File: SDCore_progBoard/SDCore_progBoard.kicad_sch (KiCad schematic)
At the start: 7 parts, among them U1 BL1117-33CX

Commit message: Updated BOOTSEL logic
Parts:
- added SW1: TS-1101-C-W, JLCImport:TS-1101-C-W, symbol JLCImport:TS-1101-C-W
- renumbered USB2 to USB1
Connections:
- net +3V3: now also SW1.1; no longer Card1.6 (VSS2)
- new net: Card1.6 (VSS2), SW1.2
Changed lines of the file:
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@@
 		(dnp no)
 		(fields_autoplaced yes)
-		(property "Reference" "USB2"
+		(property "Reference" "USB1"
 			(at 50.165 29.21 0)
 			(effects
@@
 			(project ""
 				(path "/953ecaf1-4dee-412f-b3a8-cd4cd6a046bb"
-					(reference "USB2")
+					(reference "USB1")
 					(unit 1)
 				)
@@
 	)
 	(symbol
+		(lib_id "JLCImport:TS-1101-C-W")
+		(at 124.46 63.5 90)
+		(unit 1)
+		(exclude_from_sim no)
+		(in_bom yes)
+		(on_board yes)
+		(dnp no)
+		(fields_autoplaced yes)
+		(property "Reference" "SW1"
+			(at 125.73 62.2299 90)
+			(effects
+				(font
+					(size 1.27 1.27)
+				)
+				(justify right)
+			)
+		)
+		(property "Value" "TS-1101-C-W"
+			(at 125.73 64.7699 90)
+			(effects
+				(font
+					(size 1.27 1.27)
+				)
+				(justify right)
+			)
+		)
+		(property "Footprint" "JLCImport:TS-1101-C-W"
+			(at 124.46 63.5 0)
+			(effects
+				(font
+					(size 1.27 1.27)
+				)
+				(hide yes)
+			)
+		)
+		(property "Datasheet" "https://www.lcsc.com/datasheet/lcsc_datasheet_2002271735_XKB-Connection-TS-1101-C-W_C318938.pdf"
+			(at 124.46 63.5 0)
+			(effects
+				(font
+					(size 1.27 1.27)
+				)
+				(hide yes)
+			)
+		)
+		(property "Description" "-30℃~+85℃ 12V 2.5mm 2.6N 3.6mm 50,000 cycles 50mA 6mm No Rectangular Button SPST Surface Mount,Vertical Without Bracket SMD,6x3.6mm Tactile Switches ROHS"
+			(at 124.46 63.5 0)
+			(effects
+				(font
+					(size 1.27 1.27)
+				)
+				(hide yes)
+			)
+		)
+		(property "LCSC" "C318938"
+			(at 124.46 63.5 0)
+			(effects
+				(font
+					(size 1.27 1.27)
+				)
+				(hide yes)
+			)
+		)
+		(property "Manufacturer" "XKB Connection"
+			(at 124.46 63.5 0)
+			(effects
+				(font
+					(size 1.27 1.27)
+				)
+				(hide yes)
+			)
+		)
+		(property "Manufacturer Part" "TS-1101-C-W"
+			(at 124.46 63.5 0)
+			(effects
+				(font
+					(size 1.27 1.27)
+				)
+				(hide yes)
+			)
+		)
+		(pin "1"
+		)
+		(pin "2"
+		)
+		(instances
+			(project ""
+				(path "/953ecaf1-4dee-412f-b3a8-cd4cd6a046bb"
+					(reference "SW1")
+					(unit 1)
+				)
+			)
+		)
+	)
+	(symbol
 		(lib_id "power:+3V3")
 		(at 73.66 76.2 90)
@@
 		(on_board yes)
 		(dnp no)
-		(fields_autoplaced yes)
 		(property "Reference" "#PWR017"
 			(at 77.47 76.2 0)
@@
 		)
 		(property "Value" "+3V3"
-			(at 69.85 76.1999 90)
+			(at 71.12 77.724 90)
 			(effects
 				(font
@@
 		)
 		(property "Value" "5.1k"
-			(at 64.008 67.056 0)
+			(at 70.104 62.484 0)
 			(effects
 				(font
@@
 	(symbol
 		(lib_id "power:+3V3")
-		(at 124.46 55.88 270)
+		(at 124.46 71.12 270)
 		(unit 1)
 		(exclude_from_sim no)
@@
 		(fields_autoplaced yes)
 		(property "Reference" "#PWR01"
-			(at 120.65 55.88 0)
+			(at 120.65 71.12 0)
 			(effects
 				(font
@@
 		)
 		(property "Value" "+3V3"
-			(at 128.27 55.8799 90)
+			(at 128.27 71.1199 90)
 			(effects
 				(font
@@
 		)
 		(property "Footprint" ""
-			(at 124.46 55.88 0)
+			(at 124.46 71.12 0)
 			(effects
 				(font
@@
 		)
 		(property "Datasheet" ""
-			(at 124.46 55.88 0)
+			(at 124.46 71.12 0)
 			(effects
 				(font
@@
 		)
 		(property "Description" "Power symbol creates a global label with name \"+3V3\""
-			(at 124.46 55.88 0)
+			(at 124.46 71.12 0)
 			(effects
 				(font
@@
 		(dnp no)
 		(property "Reference" "R2"
-			(at 63.5 51.816 0)
+			(at 63.246 47.244 0)
 			(effects
 				(font
@@
 		)
 		(property "Value" "5.1k"
-			(at 62.992 47.244 0)
-			(effects
-				(font
+			(at 69.596 47.244 0)
+			(effects
+				(font

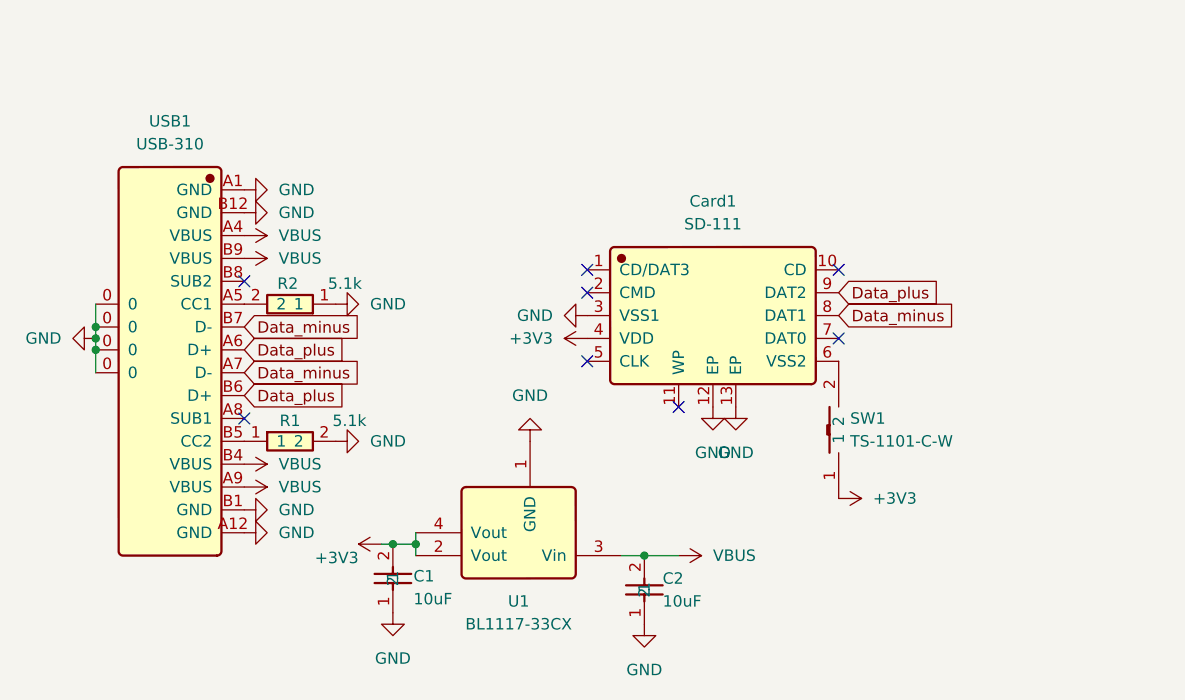
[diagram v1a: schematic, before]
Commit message: Changed entirety of the progboard design to include a pin header, to make this devboard actually useful
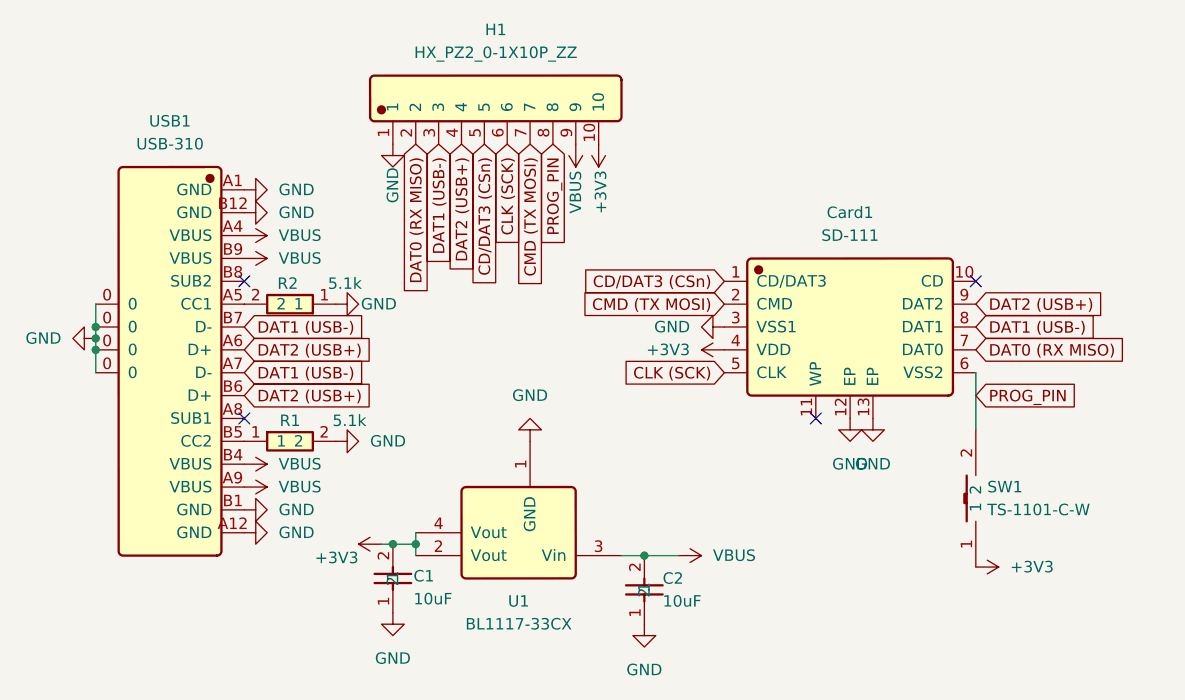
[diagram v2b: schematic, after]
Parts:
- added H1: HX_PZ2_0-1X10P_ZZ, JLCImport:HX_PZ2_0-1X10P_ZZ, symbol JLCImport:HX_PZ2_0-1X10P_ZZ
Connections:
- net +3V3: now also H1.10
- net GND: now also H1.1
- net VBUS: now also H1.9
- net CD/DAT3 (CSn): now reaches Card1.1 (CD/DAT3)
- net CD/DAT3 (CSn): now also H1.5
- net CMD (TX MOSI): now reaches Card1.2 (CMD)
- net CMD (TX MOSI): now also H1.7
- net CLK (SCK): now reaches Card1.5 (CLK)
- net CLK (SCK): now also H1.6
- net PROG_PIN: now reaches Card1.6 (VSS2), SW1.2
- net PROG_PIN: now also H1.8
- net DAT0 (RX MISO): now reaches Card1.7 (DAT0)
- net DAT0 (RX MISO): now also H1.2
- net Data_minus renamed DAT1 (USB-)
- net DAT1 (USB-): now also H1.3
- net Data_plus renamed DAT2 (USB+)
- net DAT2 (USB+): now also H1.4
- no-connect marks 8 -> 4
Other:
- moved on the sheet: Card1, SW1
